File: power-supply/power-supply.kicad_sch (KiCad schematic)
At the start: 27 parts, among them J1 Barrel_Jack, J2 Output, J3 Output, SW1 SW_SPDT, U1 L7812, U2 L7912, U3 L7805

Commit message: Update power supply
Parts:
- C10, C11, C12, C7, C8, C9: footprint Capacitor_THT:C_Disc_D5.0mm_W2.5mm_P5.00mm -> Capacitor_THT:CP_Radial_Tantal_D4.5mm_P2.50mm
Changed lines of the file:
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@@
 			)
 		)
-		(property "Footprint" "Capacitor_THT:C_Disc_D5.0mm_W2.5mm_P5.00mm"
+		(property "Footprint" "Capacitor_THT:CP_Radial_Tantal_D4.5mm_P2.50mm"
 			(at 170.18 110.49 0)
 			(effects
@@
 			)
 		)
-		(property "Footprint" "Capacitor_THT:C_Disc_D5.0mm_W2.5mm_P5.00mm"
+		(property "Footprint" "Capacitor_THT:CP_Radial_Tantal_D4.5mm_P2.50mm"
 			(at 170.18 87.63 0)
 			(effects
@@
 			)
 		)
-		(property "Footprint" "Capacitor_THT:C_Disc_D5.0mm_W2.5mm_P5.00mm"
+		(property "Footprint" "Capacitor_THT:CP_Radial_Tantal_D4.5mm_P2.50mm"
 			(at 139.7 110.49 0)
 			(effects
@@
 			)
 		)
-		(property "Footprint" "Capacitor_THT:C_Disc_D5.0mm_W2.5mm_P5.00mm"
+		(property "Footprint" "Capacitor_THT:CP_Radial_Tantal_D4.5mm_P2.50mm"
 			(at 224.79 39.37 0)
 			(effects
@@
 			)
 		)
-		(property "Footprint" "Capacitor_THT:C_Disc_D5.0mm_W2.5mm_P5.00mm"
+		(property "Footprint" "Capacitor_THT:CP_Radial_Tantal_D4.5mm_P2.50mm"
 			(at 259.08 39.37 0)
 			(effects
@@
 			)
 		)
-		(property "Footprint" "Capacitor_THT:C_Disc_D5.0mm_W2.5mm_P5.00mm"
+		(property "Footprint" "Capacitor_THT:CP_Radial_Tantal_D4.5mm_P2.50mm"
 			(at 139.7 87.63 0)
 			(effects

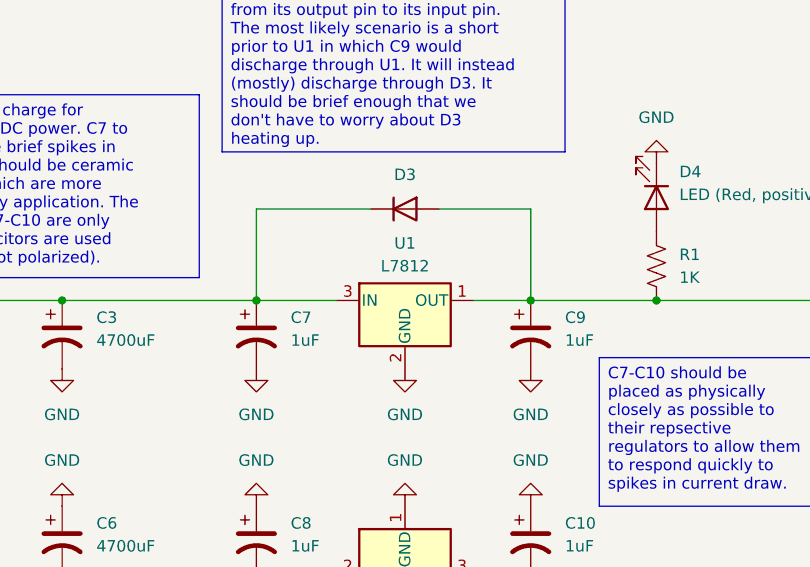
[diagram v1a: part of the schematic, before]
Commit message: Fix L812 orientation in power supply
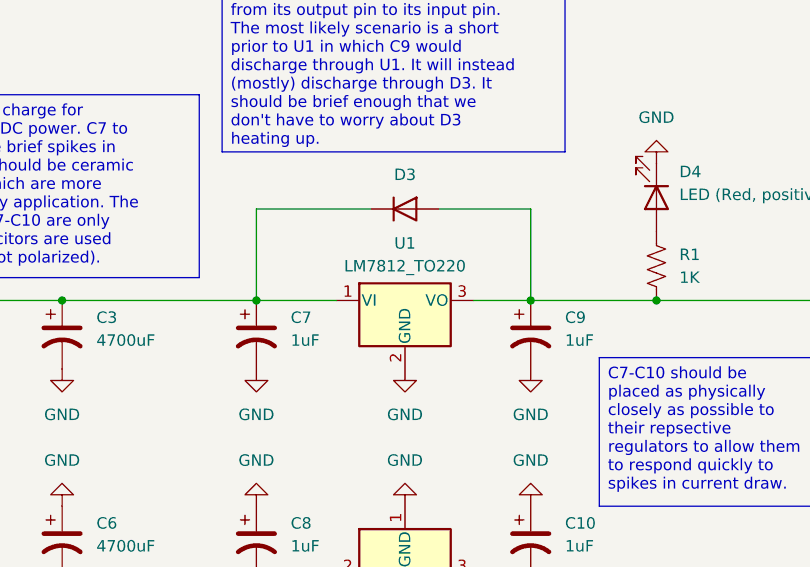
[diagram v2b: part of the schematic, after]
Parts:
- removed U1: L7812, Package_TO_SOT_THT:TO-220-3_Vertical, symbol Regulator_Linear:L78L12_SOT89
- added U1: LM7812_TO220, Package_TO_SOT_THT:TO-220-3_Vertical, symbol Regulator_Linear:LM7812_TO220
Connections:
- net GND: now also U1.2 (GND)
- net at C1.1, C2.1, C3.1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: now also U1.1 (VI)
- net at C11.1, C9.1, D3.2 (A)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: now also U1.3 (VO)
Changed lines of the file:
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@@
+	)
+	(symbol
+		(lib_id "Regulator_Linear:LM7812_TO220")
+		(at 156.21 83.82 0)
+		(unit 1)
+		(exclude_from_sim no)
+		(in_bom yes)
+		(on_board yes)
+		(dnp no)
+		(fields_autoplaced yes)
+		(property "Reference" "U1"
+			(at 156.21 77.47 0)
+			(effects
+				(font
+					(size 1.27 1.27)
+				)
+			)
+		)
+		(property "Value" "LM7812_TO220"
+			(at 156.21 80.01 0)
+			(effects
+				(font
+					(size 1.27 1.27)
+				)
+			)
+		)
+		(property "Footprint" "Package_TO_SOT_THT:TO-220-3_Vertical"
+			(at 156.21 78.105 0)
+			(effects
+				(font
+					(size 1.27 1.27)
+					(italic yes)
+				)
+				(hide yes)
+			)
+		)
+		(property "Datasheet" "https://www.onsemi.cn/PowerSolutions/document/MC7800-D.PDF"
+			(at 156.21 85.09 0)
+			(effects
+				(font
+					(size 1.27 1.27)
+				)
+				(hide yes)
+			)
+		)
+		(property "Description" "Positive 1A 35V Linear Regulator, Fixed Output 12V, TO-220"
+			(at 156.21 83.82 0)
+			(effects
+				(font
+					(size 1.27 1.27)
+				)
+				(hide yes)
+			)
+		)
+		(pin "1"
+		)
+		(pin "3"
+		)
+		(pin "2"
+		)
+		(instances
+			(project ""
+				(path "/71e7480b-4148-4d0b-bbe2-57d9a5092859"
+					(reference "U1")
+					(unit 1)
+				)
+			)
+		)
 	)
 	(symbol
@@
 					(unit 1)
 				)
-			)
-		)
-	)
-	(symbol
-		(lib_id "Regulator_Linear:L78L12_SOT89")
-		(at 156.21 83.82 0)
-		(unit 1)
-		(exclude_from_sim no)
-		(in_bom yes)
-		(on_board yes)
-		(dnp no)
-		(fields_autoplaced yes)
-		(property "Reference" "U1"
-			(at 156.21 77.47 0)
-			(effects
-				(font
-					(size 1.27 1.27)
-				)
-			)
-		)
-		(property "Value" "L7812"
-			(at 156.21 80.01 0)
-			(effects
-				(font
-					(size 1.27 1.27)
-				)
-			)
-		)
-		(property "Footprint" "Package_TO_SOT_THT:TO-220-3_Vertical"
-			(at 156.21 78.74 0)
-			(effects
-				(font
-					(size 1.27 1.27)
-					(italic yes)
-				)
-				(hide yes)
-			)
-		)
-		(property "Datasheet" "http://www.st.com/content/ccc/resource/technical/document/datasheet/15/55/e5/aa/23/5b/43/fd/CD00000446.pdf/files/CD00000446.pdf/jcr:content/translations/en.CD00000446.pdf"
-			(at 156.21 85.09 0)
-			(effects
-				(font
-					(size 1.27 1.27)
-				)
-				(hide yes)
-			)
-		)
-		(property "Description" "Positive 100mA 30V Linear Regulator, Fixed Output 12V, SOT-89"
-			(at 156.21 83.82 0)
-			(effects
-				(font
-					(size 1.27 1.27)
-				)
-				(hide yes)
-			)
-		)
-		(pin "1"
-		)
-		(pin "2"
-		)
-		(pin "3"
-		)
-		(instances
-			(project "power-supply"
-				(path "/71e7480b-4148-4d0b-bbe2-57d9a5092859"
-					(reference "U1")
-					(unit 1)
-				)

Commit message: Various improvements
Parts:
- added J4: Output, Connector_IDC:IDC-Header_2x03_P2.54mm_Vertical, symbol Connector_Generic:Conn_02x03_Odd_Even
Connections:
- net GND: now also J4.3 (Pin_3), J4.4 (Pin_4)
- net at C10.2, J2.2 (Pin_2), J3.2 (Pin_2)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: now also J4.2 (Pin_2)
- net at C11.1, C9.1, D3.2 (A)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: now also J4.1 (Pin_1)
- net at C12.1, D6.2 (A), J2.5 (Pin_5)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: now also J4.5 (Pin_5)
- no-connect marks 3 -> 4
